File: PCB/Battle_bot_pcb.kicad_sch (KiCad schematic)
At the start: 0 parts

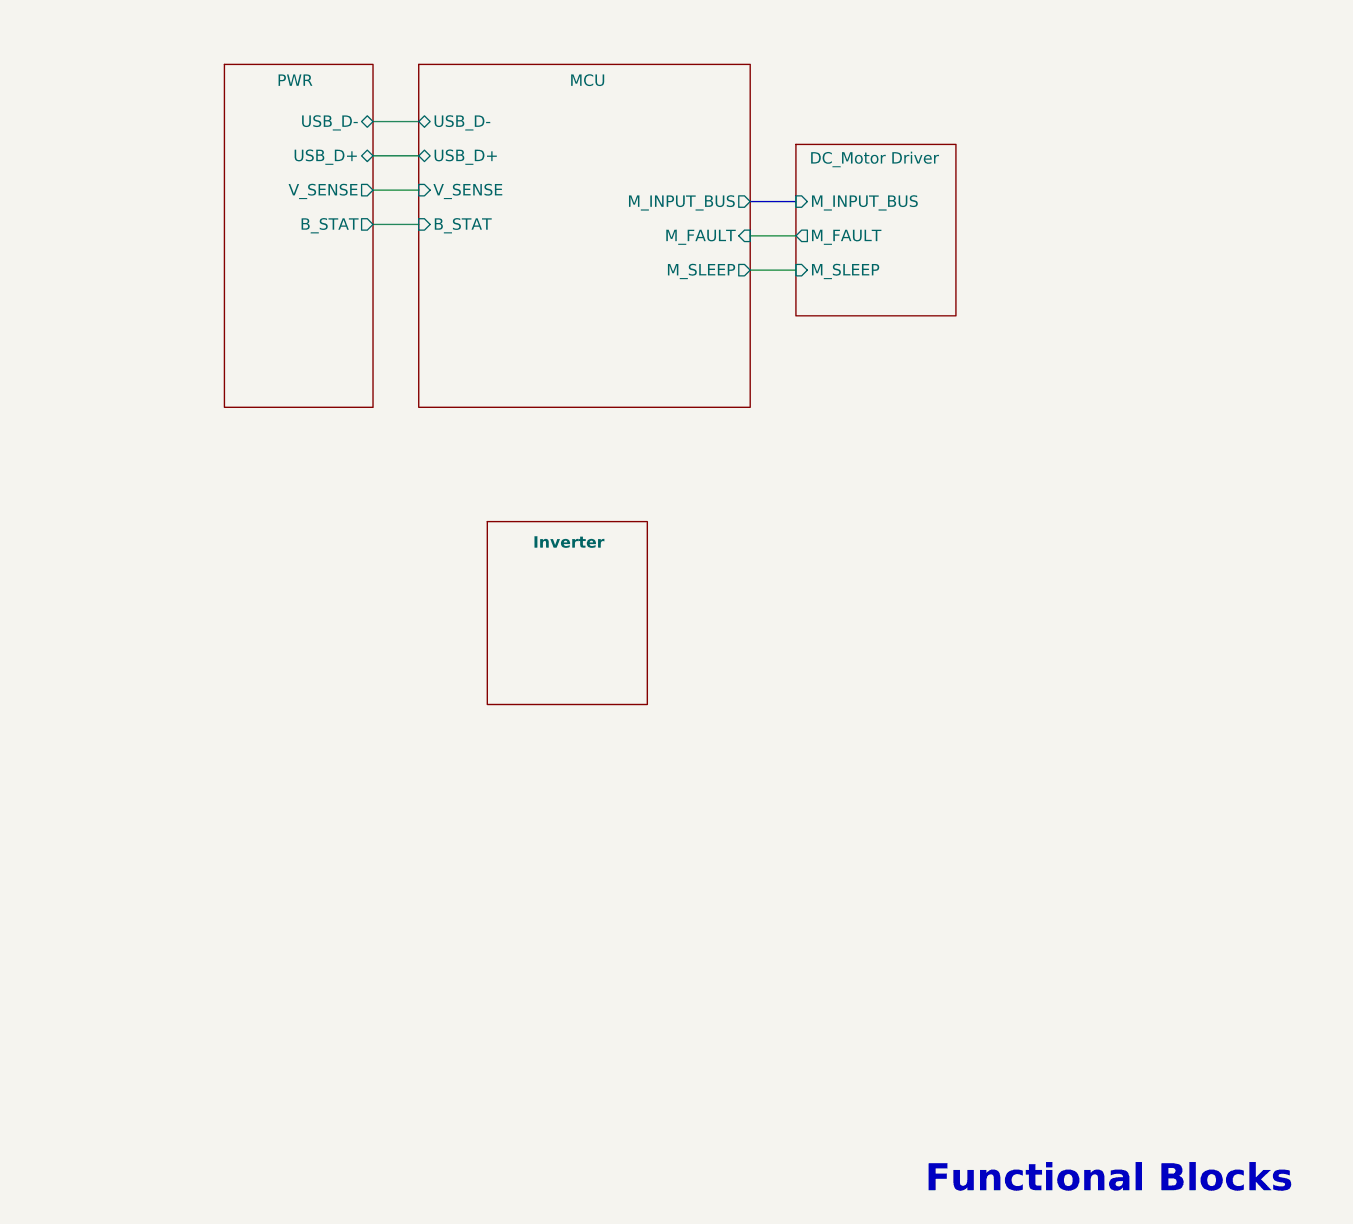
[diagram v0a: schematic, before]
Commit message: Started design of Inverter
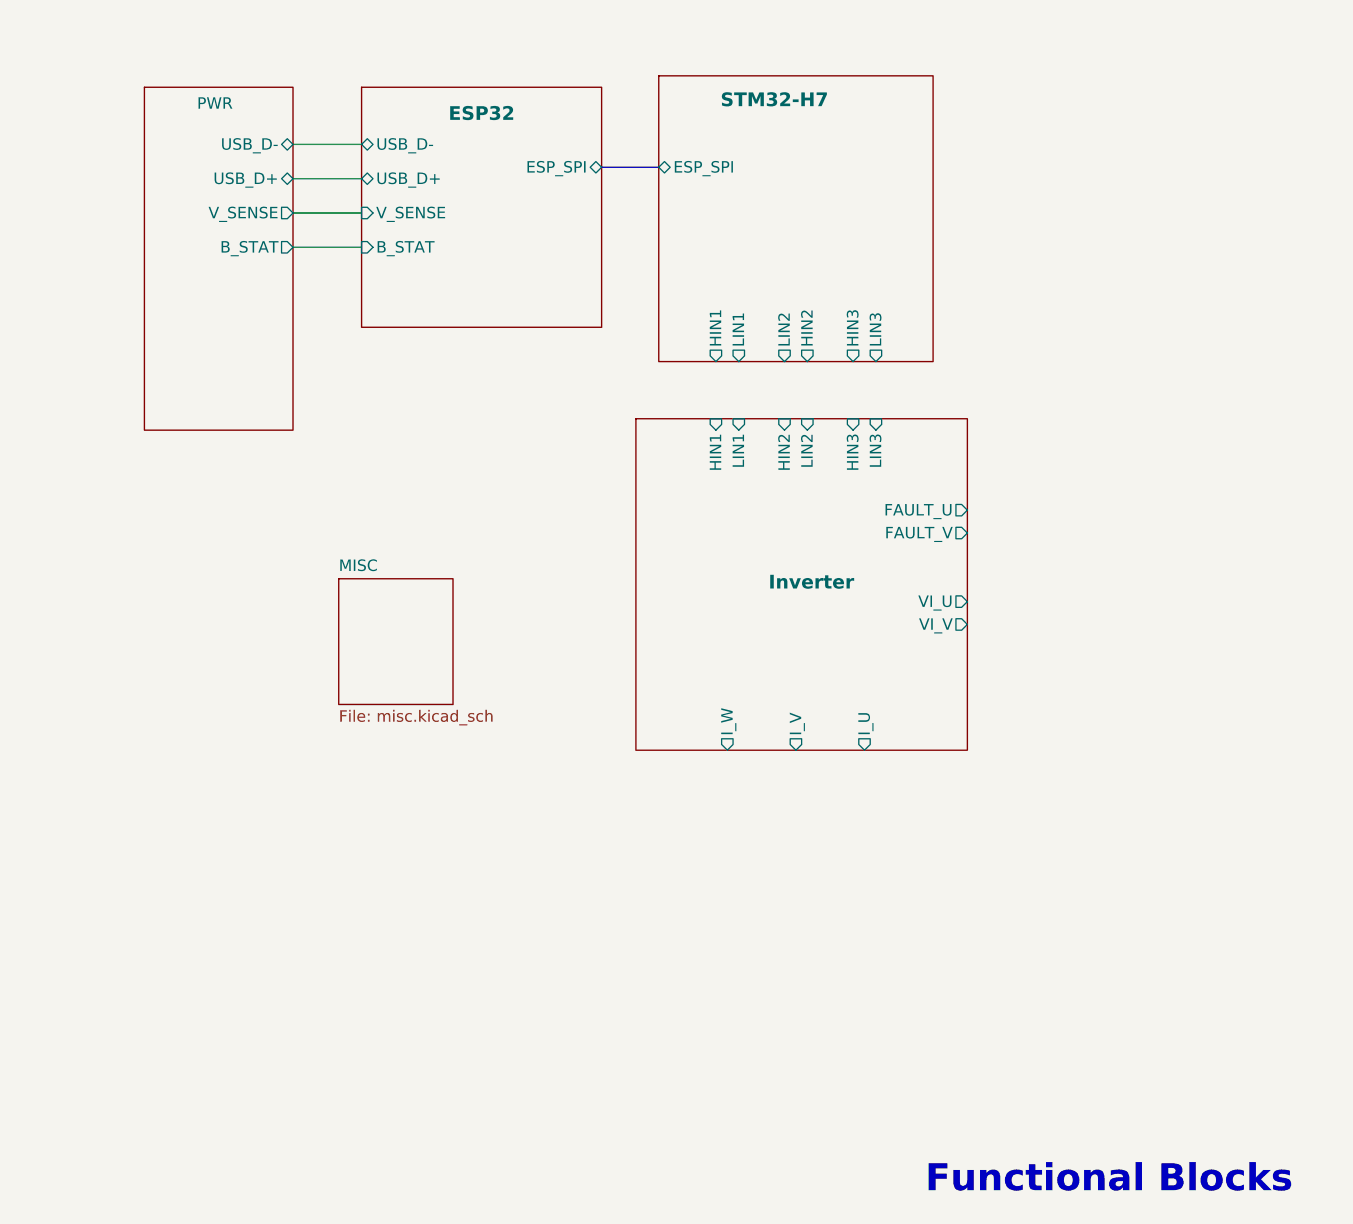
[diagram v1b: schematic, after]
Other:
- sheet MCU renamed ESP32
- removed sheet DC_Motor Driver
- added sheet MISC (misc.kicad_sch)
- added sheet STM32-H7 (MCU.kicad_sch)
- sheet ESP32 ports: added ESP_SPI; removed M_FAULT, M_INPUT_BUS, M_SLEEP
- sheet Inverter ports: added FAULT_U, FAULT_V, HIN1, HIN2, HIN3, I_U, I_V, I_W, LIN1, LIN2, LIN3, VI_U, VI_V; removed none

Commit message: Hardware updates: STM32H7 and Inverted design
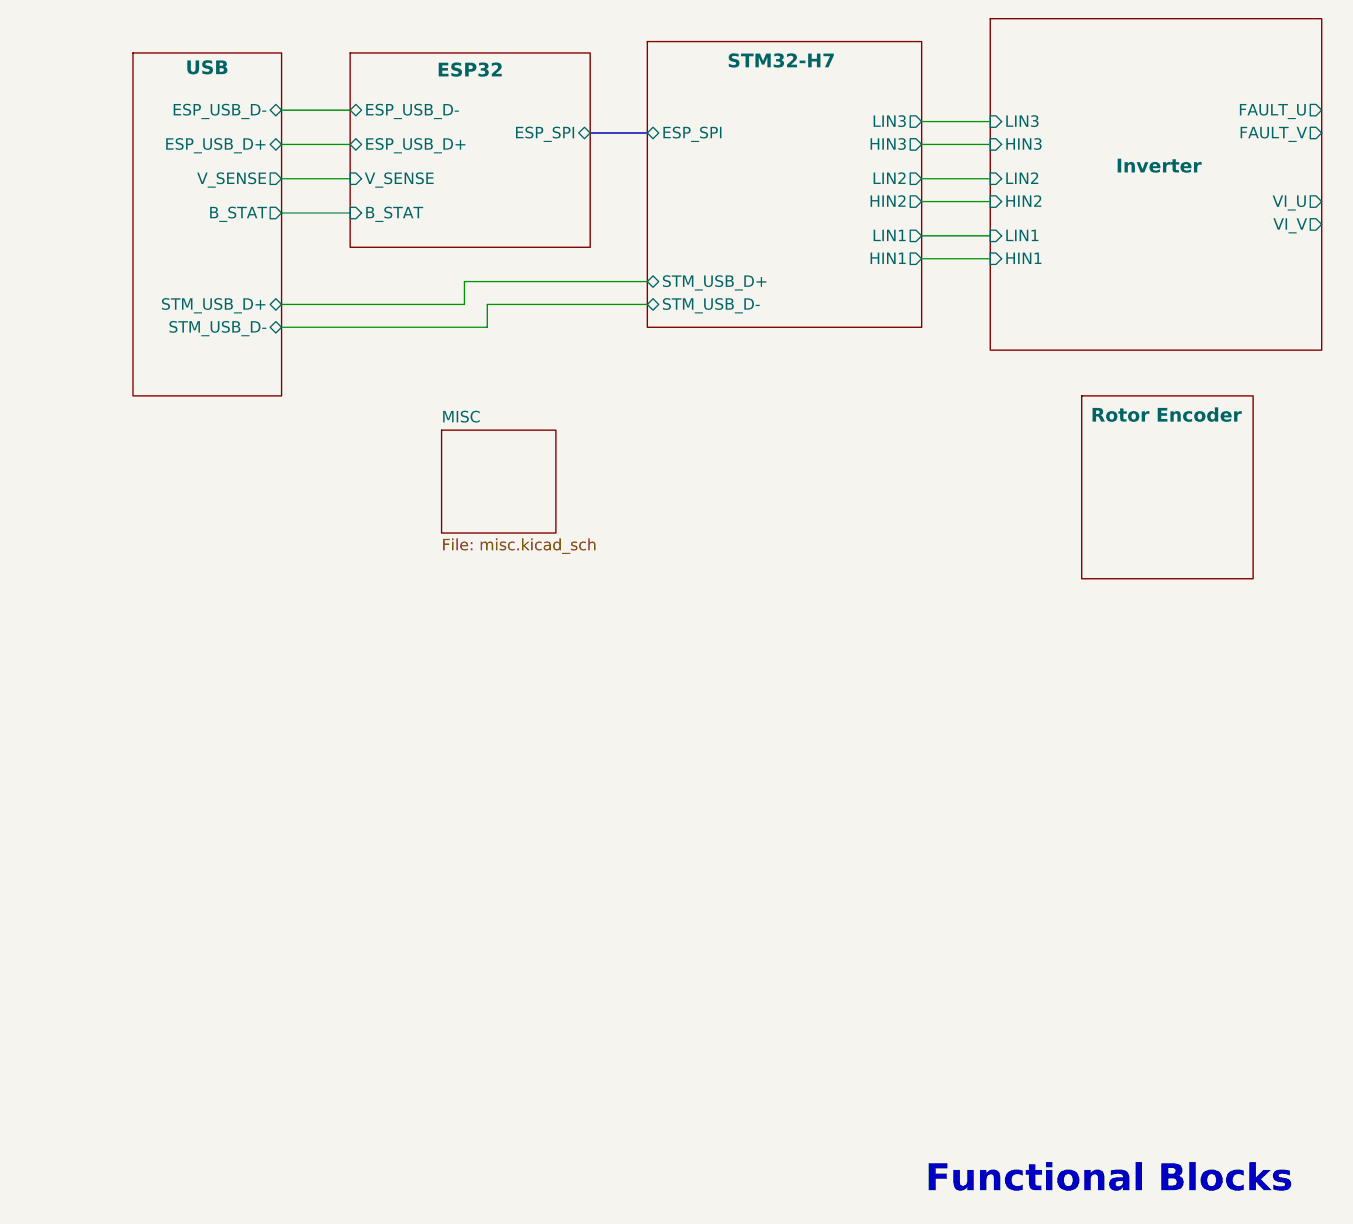
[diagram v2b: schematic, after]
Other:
- sheet PWR renamed USB
- added sheet Rotor Encoder (estimator.kicad_sch)
- sheet ESP32 ports: added ESP_USB_D+, ESP_USB_D-; removed USB_D+, USB_D-
- sheet Inverter ports: added none; removed I_U, I_V, I_W
- sheet STM32-H7 ports: added STM_USB_D+, STM_USB_D-; removed none
- sheet USB ports: added ESP_USB_D+, ESP_USB_D-, STM_USB_D+, STM_USB_D-; removed USB_D+, USB_D-

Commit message: Latest PCB version
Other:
- sheet Inverter renamed Inverter motor controller
- added sheet SD-Card (sd.kicad_sch)
